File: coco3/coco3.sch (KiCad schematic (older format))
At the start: 8 parts, among them CN1 Conn_02x20_Odd_Even

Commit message: -repplaced a whole bunch of THT components with SMT components
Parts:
- C26: footprint Capacitor_THT:C_Disc_D4.7mm_W2.5mm_P5.00mm -> Capacitor_SMD:C_0805_2012Metric_Pad1.18x1.45mm_HandSolder; Manufacturer part# FG28C0G1H103JNT06 -> CL21A106KAYNNNE; Vendor digikey -> JLCPCB; Vendor part# 445-173474-1-ND -> C15850
- C27: footprint Capacitor_THT:CP_Radial_D8.0mm_P5.00mm -> Capacitor_SMD:CP_Elec_6.3x5.3; Manufacturer part# UST1C101MDD1TA -> VEJ101M1CTR-0605; Vendor digikey -> JLCPCB; Vendor part# 493-17434-1-ND -> C164064
- C61: footprint Capacitor_THT:C_Disc_D4.7mm_W2.5mm_P5.00mm -> Capacitor_SMD:C_0805_2012Metric_Pad1.18x1.45mm_HandSolder; Manufacturer part# K390J15C0GF5TL2 -> 0805N390J500CT; Vendor digikey -> JLCPCB; Vendor part# BC1008CT-ND -> C296098
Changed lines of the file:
@@
 F 0 "C26" H 1850 3700 50  0000 C CNN
 F 1 ".1uF" H 1900 3900 50  0000 C CNN
-F 2 "Capacitor_THT:C_Disc_D4.7mm_W2.5mm_P5.00mm" H 2000 3800 50  0001 C CNN
-F 3 " https://product.tdk.com/info/en/catalog/datasheets/leadmlcc_halogenfree_fg_en.pdf?ref_disty=digikey" H 2000 3800 50  0001 C CNN
-F 4 "digikey" V 2000 3800 50  0001 C CNN "Vendor"
-F 5 "445-173474-1-ND" V 2000 3800 50  0001 C CNN "Vendor part#"
-F 6 "FG28C0G1H103JNT06" V 2000 3800 50  0001 C CNN "Manufacturer part#"
+F 2 "Capacitor_SMD:C_0805_2012Metric_Pad1.18x1.45mm_HandSolder" H 2000 3800 50  0001 C CNN
+F 3 "https://datasheet.lcsc.com/lcsc/1811121310_Samsung-Electro-Mechanics-CL21A106KAYNNNE_C15850.pdf" H 2000 3800 50  0001 C CNN
+F 4 "JLCPCB" V 2000 3800 50  0001 C CNN "Vendor"
+F 5 "C15850" V 2000 3800 50  0001 C CNN "Vendor part#"
+F 6 "CL21A106KAYNNNE" V 2000 3800 50  0001 C CNN "Manufacturer part#"
 	1    2000 3800
 	-1   0    0    1
@@
 F 0 "C27" H 1500 3650 50  0000 L CNN
 F 1 "100uF 16v" H 1800 3600 50  0000 L CNN
-F 2 "Capacitor_THT:CP_Radial_D8.0mm_P5.00mm" H 1700 3800 50  0001 C CNN
-F 3 "http://nichicon-us.com/english/products/pdfs/e-uvz.pdf" H 1700 3800 50  0001 C CNN
-F 4 "digikey" H 1700 3800 50  0001 C CNN "Vendor"
-F 5 "493-17434-1-ND" H 1700 3800 50  0001 C CNN "Vendor part#"
-F 6 "UST1C101MDD1TA" H 1700 3800 50  0001 C CNN "Manufacturer part#"
+F 2 "Capacitor_SMD:CP_Elec_6.3x5.3" H 1700 3800 50  0001 C CNN
+F 3 "https://datasheet.lcsc.com/lcsc/1811051603_Lelon-VEJ101M1CTR-0605_C164064.pdf" H 1700 3800 50  0001 C CNN
+F 4 "JLCPCB" H 1700 3800 50  0001 C CNN "Vendor"
+F 5 "C164064" H 1700 3800 50  0001 C CNN "Vendor part#"
+F 6 "VEJ101M1CTR-0605" H 1700 3800 50  0001 C CNN "Manufacturer part#"
 	1    1700 3800
 	-1   0    0    1
@@
 F 0 "C61" H 3850 5200 50  0000 C CNN
 F 1 "39pF" H 3900 5400 50  0000 C CNN
-F 2 "Capacitor_THT:C_Disc_D4.7mm_W2.5mm_P5.00mm" H 3750 5300 50  0001 C CNN
-F 3 " https://www.vishay.com/docs/45171/kseries.pdf" H 3750 5300 50  0001 C CNN
-F 4 "digikey" V 3750 5300 50  0001 C CNN "Vendor"
-F 5 "BC1008CT-ND" V 3750 5300 50  0001 C CNN "Vendor part#"
-F 6 "K390J15C0GF5TL2" V 3750 5300 50  0001 C CNN "Manufacturer part#"
+F 2 "Capacitor_SMD:C_0805_2012Metric_Pad1.18x1.45mm_HandSolder" H 3750 5300 50  0001 C CNN
+F 3 "https://datasheet.lcsc.com/lcsc/1810191333_Walsin-Tech-Corp-0805N390J500CT_C296098.pdf" H 3750 5300 50  0001 C CNN
+F 4 "JLCPCB" V 3750 5300 50  0001 C CNN "Vendor"
+F 5 "C296098" V 3750 5300 50  0001 C CNN "Vendor part#"
+F 6 "0805N390J500CT" V 3750 5300 50  0001 C CNN "Manufacturer part#"
 	1    3750 5300
 	1    0    0    1

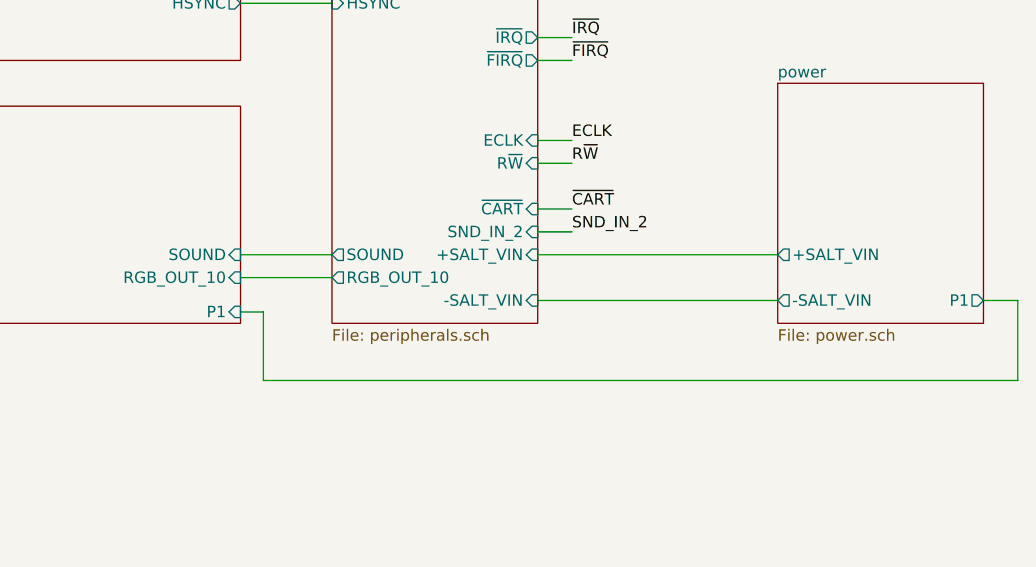
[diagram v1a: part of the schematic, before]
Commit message: -converted more components from THT to SMD -replaced SALT chip with replacement circuitry
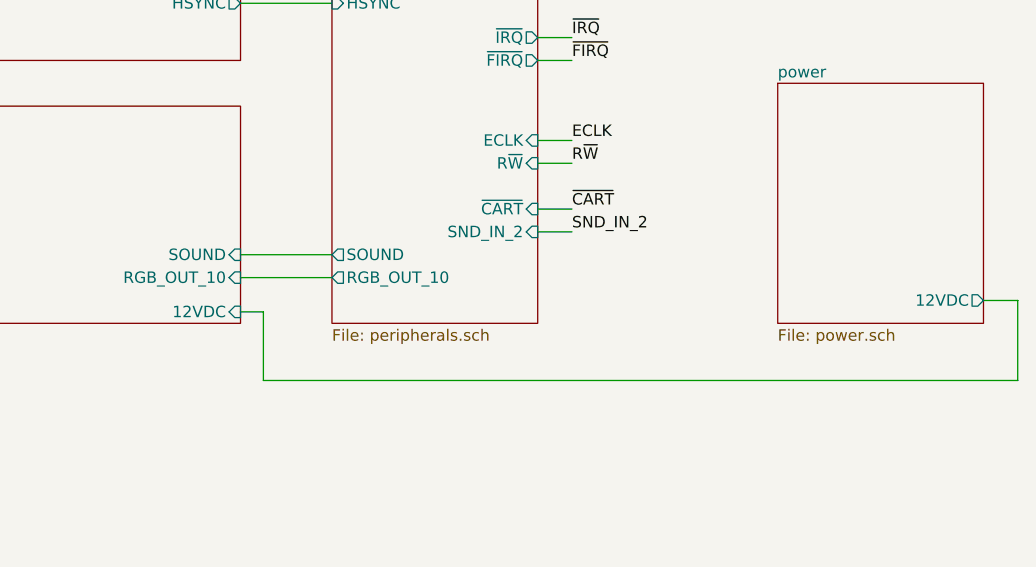
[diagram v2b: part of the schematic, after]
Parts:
- R64: footprint Resistor_THT:R_Axial_DIN0207_L6.3mm_D2.5mm_P10.16mm_Horizontal -> Resistor_SMD:R_1206_3216Metric_Pad1.30x1.75mm_HandSolder; Manufacturer part# CF14JT47R0 -> 1206W4J0470T5E; Vendor digikey -> JLCPCB; Vendor part# CF14JT47R0CT-ND -> C25384
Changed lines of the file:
@@
 F0 "power" 50
 F1 "power.sch" 50
-F2 "-SALT_VIN" O L 9000 5750 50
-F3 "+SALT_VIN" O L 9000 5550 50
-F4 "P1" O R 9900 5750 50
+F2 "12VDC" O R 9900 5750 50
 $EndSheet
 Wire Bus Line
@@
 Wire Bus Line
 	850  1450 3550 1450
-Wire Wire Line
-	7950 5550 9000 5550
-Wire Wire Line
-	9000 5750 7950 5750
 Wire Wire Line
 	2150 2150 1950 2150
@@
 F0 "peripherals" 50
 F1 "peripherals.sch" 50
-F2 "-SALT_VIN" I R 7950 5750 50
-F3 "+SALT_VIN" I R 7950 5550 50
-F4 "D[0..7]" B R 7950 4300 50
-F5 "R~W" I R 7950 5150 50
-F6 "~IRQ" O R 7950 4600 50
-F7 "~RESET" I R 7950 4200 50
-F8 "A[0..15]" I R 7950 4400 50
-F9 "~CART" I R 7950 5350 50
-F10 "~FIRQ" O R 7950 4700 50
-F11 "SERINT" O L 7050 4050 50
-F12 "RGB_OUT_10" O L 7050 5650 50
-F13 "PIA_~CS2" I L 7050 4250 50
-F14 "ECLK" I R 7950 5050 50
-F15 "IL1" O L 7050 4150 50
-F16 "SND_IN_2" I R 7950 5450 50
-F17 "~VSYNC" I L 7050 4350 50
-F18 "~HSYNC" I L 7050 4450 50
-F19 "SOUND" O L 7050 5550 50
+F2 "D[0..7]" B R 7950 4300 50
+F3 "R~W" I R 7950 5150 50
+F4 "~IRQ" O R 7950 4600 50
+F5 "~RESET" I R 7950 4200 50
+F6 "A[0..15]" I R 7950 4400 50
+F7 "~CART" I R 7950 5350 50
+F8 "~FIRQ" O R 7950 4700 50
+F9 "SERINT" O L 7050 4050 50
+F10 "RGB_OUT_10" O L 7050 5650 50
+F11 "PIA_~CS2" I L 7050 4250 50
+F12 "ECLK" I R 7950 5050 50
+F13 "IL1" O L 7050 4150 50
+F14 "SND_IN_2" I R 7950 5450 50
+F15 "~VSYNC" I L 7050 4350 50
+F16 "~HSYNC" I L 7050 4450 50
+F17 "SOUND" O L 7050 5550 50
 $EndSheet
 Wire Bus Line
@@
 F8 "VSYNC" I L 4600 5500 50
 F9 "SOUND" I R 6650 5550 50
-F10 "P1" I R 6650 5800 50
+F10 "12VDC" I R 6650 5800 50
 $EndSheet
 Wire Wire Line
@@
 F 0 "R64" V 3900 4850 50  0000 L CNN
 F 1 "47" V 3900 5100 50  0000 L CNN
-F 2 "Resistor_THT:R_Axial_DIN0207_L6.3mm_D2.5mm_P10.16mm_Horizontal" H 3850 5100 50  0001 C CNN
-F 3 "https://www.seielect.com/catalog/sei-cf_cfm.pdf" H 3850 5100 50  0001 C CNN
-F 4 "digikey" H 3850 5100 50  0001 C CNN "Vendor"
-F 5 "CF14JT47R0CT-ND" H 3850 5100 50  0001 C CNN "Vendor part#"
-F 6 "CF14JT47R0" H 3850 5100 50  0001 C CNN "Manufacturer part#"
+F 2 "Resistor_SMD:R_1206_3216Metric_Pad1.30x1.75mm_HandSolder" H 3850 5100 50  0001 C CNN
+F 3 "https://datasheet.lcsc.com/lcsc/1811101020_UNI-ROYAL-Uniroyal-Elec-1206W4J0470T5E_C25384.pdf" H 3850 5100 50  0001 C CNN
+F 4 "JLCPCB" H 3850 5100 50  0001 C CNN "Vendor"
+F 5 "C25384" H 3850 5100 50  0001 C CNN "Vendor part#"
+F 6 " 1206W4J0470T5E" H 3850 5100 50  0001 C CNN "Manufacturer part#"
 	1    3850 5100
 	0    1    -1   0

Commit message: routed the board
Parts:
- C27: value 100uF 16v -> 100uF 6.3V; footprint Capacitor_SMD:CP_Elec_6.3x5.3 -> Capacitor_Tantalum_SMD:CP_EIA-3528-21_Kemet-B; Manufacturer part# VEJ101M1CTR-0605 -> TAJB107K006RNJ; Vendor part# C164064 -> C16133
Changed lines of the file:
@@
 AR Path="/613747DC" Ref="C27"  Part="1"
 F 0 "C27" H 1500 3650 50  0000 L CNN
-F 1 "100uF 16v" H 1800 3600 50  0000 L CNN
-F 2 "Capacitor_SMD:CP_Elec_6.3x5.3" H 1700 3800 50  0001 C CNN
-F 3 "https://datasheet.lcsc.com/lcsc/1811051603_Lelon-VEJ101M1CTR-0605_C164064.pdf" H 1700 3800 50  0001 C CNN
+F 1 "100uF 6.3V" H 1800 3600 50  0000 L CNN
+F 2 "Capacitor_Tantalum_SMD:CP_EIA-3528-21_Kemet-B" H 1700 3800 50  0001 C CNN
+F 3 "https://datasheet.lcsc.com/lcsc/1811071223_AVX-TAJB107K006RNJ_C16133.pdf" H 1700 3800 50  0001 C CNN
 F 4 "JLCPCB" H 1700 3800 50  0001 C CNN "Vendor"
-F 5 "C164064" H 1700 3800 50  0001 C CNN "Vendor part#"
-F 6 "VEJ101M1CTR-0605" H 1700 3800 50  0001 C CNN "Manufacturer part#"
+F 5 "C16133" H 1700 3800 50  0001 C CNN "Vendor part#"
+F 6 "TAJB107K006RNJ" H 1700 3800 50  0001 C CNN "Manufacturer part#"
 	1    1700 3800
 	-1   0    0    1
